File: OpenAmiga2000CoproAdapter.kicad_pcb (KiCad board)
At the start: 2 copper layers, 111.6 x 37.5 mm, 19 parts, among them CN1 A2000_COPRO_SLOT, P1 CONN_2, P10 CONN_1, P11 CONN_1, P12 CONN_1, P13 CONN_1, P14 CONN_1, P15 CONN_1, P16 CONN_1, P17 CONN_2, P2 CONN_2, P3 CONN_2, P4 CONN_2, P5 CONN_2, P6 OSHW_LOGO, P7 CONN_1, P8 CONN_1, P9 CONN_1, U1 68000D

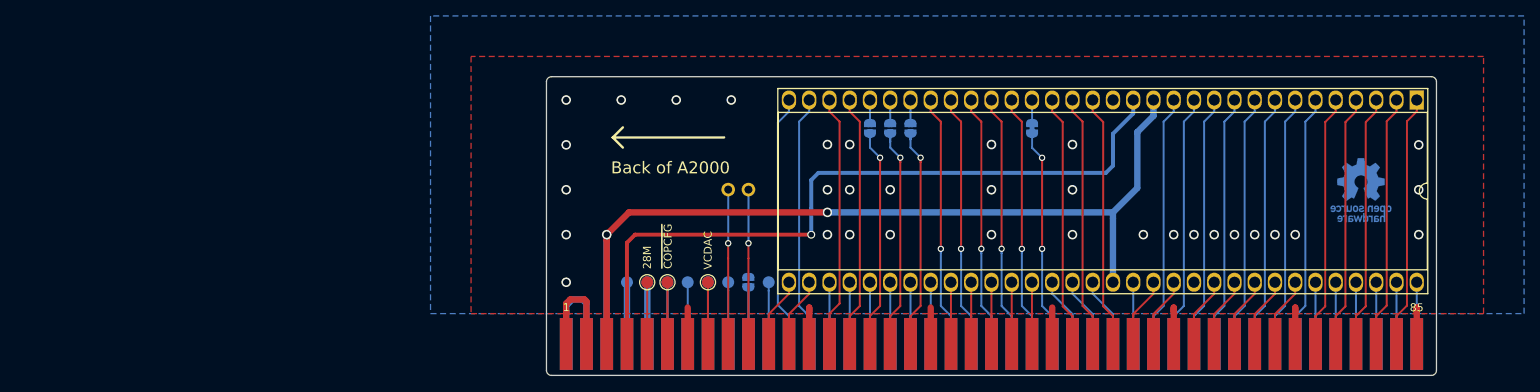
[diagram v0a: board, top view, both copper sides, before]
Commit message: Enlarged design to ensure protection against polarity reversal
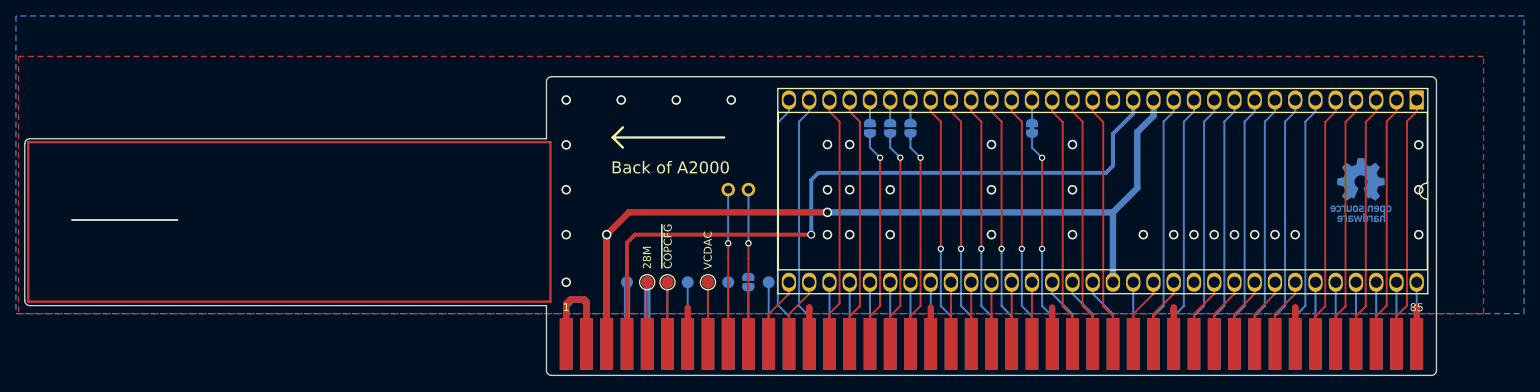
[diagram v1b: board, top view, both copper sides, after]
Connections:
- net /r_~w renamed /r_~{w}
- net /~as renamed /~{as}
- net /~berr renamed /~{berr}
- net /~bgack renamed /~{bgack}
- net /~cbg renamed /~{cbg}
- net /~cbr renamed /~{cbr}
- net /~dtack renamed /~{dtack}
- net /~hlt renamed /~{hlt}
- net /~ipl0 renamed /~{ipl0}
- net /~ipl1 renamed /~{ipl1}
- net /~ipl2 renamed /~{ipl2}
- net /~lds renamed /~{lds}
- net /~rst renamed /~{rst}
- net /~uds renamed /~{uds}
- net /~vma renamed /~{vma}
- net /~vpa renamed /~{vpa}
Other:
- board size 111.6 x 37.5 mm -> 177.1 x 37.5 mm
- net class Clock removed
- net class Default removed
- net class Power removed
- board text added: "R/~{W}"
- board text added: "~{AS}"
- board text added: "~{BERR}"
- board text added: "~{BGACK}"
- board text added: "~{BG}"
- board text added: "~{BOSS}"
- board text added: "~{BR}"
- board text added: "~{CFG_IN}"
- board text added: "~{COPCFG}"
- board text added: "~{DTACK}"
- board text added: "~{HALT}"
- board text added: "~{INT2}"
- board text added: "~{INT6}"
- board text added: "~{IPL0}"
- board text added: "~{IPL1}"
- board text added: "~{IPL2}"
- board text added: "~{LDS}"
- board text added: "~{OVR}"
- board text added: "~{RESET}"
- board text added: "~{UDS}"
- board text added: "~{VC1}"
- board text added: "~{VC3}"
- board text added: "~{VMA}"
- board text added: "~{VPA}"
- board text removed: "R/~W"
- board text removed: "~AS"
- board text removed: "~BERR"
- board text removed: "~BG"
- board text removed: "~BGACK"
- board text removed: "~BOSS"
- board text removed: "~BR"
- board text removed: "~CFG_IN"
- board text removed: "~COPCFG"
- board text removed: "~DTACK"
- board text removed: "~HALT"
- board text removed: "~INT2"
- board text removed: "~INT6"
- board text removed: "~IPL0"
- board text removed: "~IPL1"
- board text removed: "~IPL2"
- board text removed: "~LDS"
- board text removed: "~OVR"
- board text removed: "~RESET"
- board text removed: "~UDS"
- board text removed: "~VC1"
- board text removed: "~VC3"
- board text removed: "~VMA"
- board text removed: "~VPA"
